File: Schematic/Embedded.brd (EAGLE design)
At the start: 98.7 x 81.3 mm, 19 parts, among them T1 2N3904, T2 2N3904, T3 2N3904, T4 2N3904

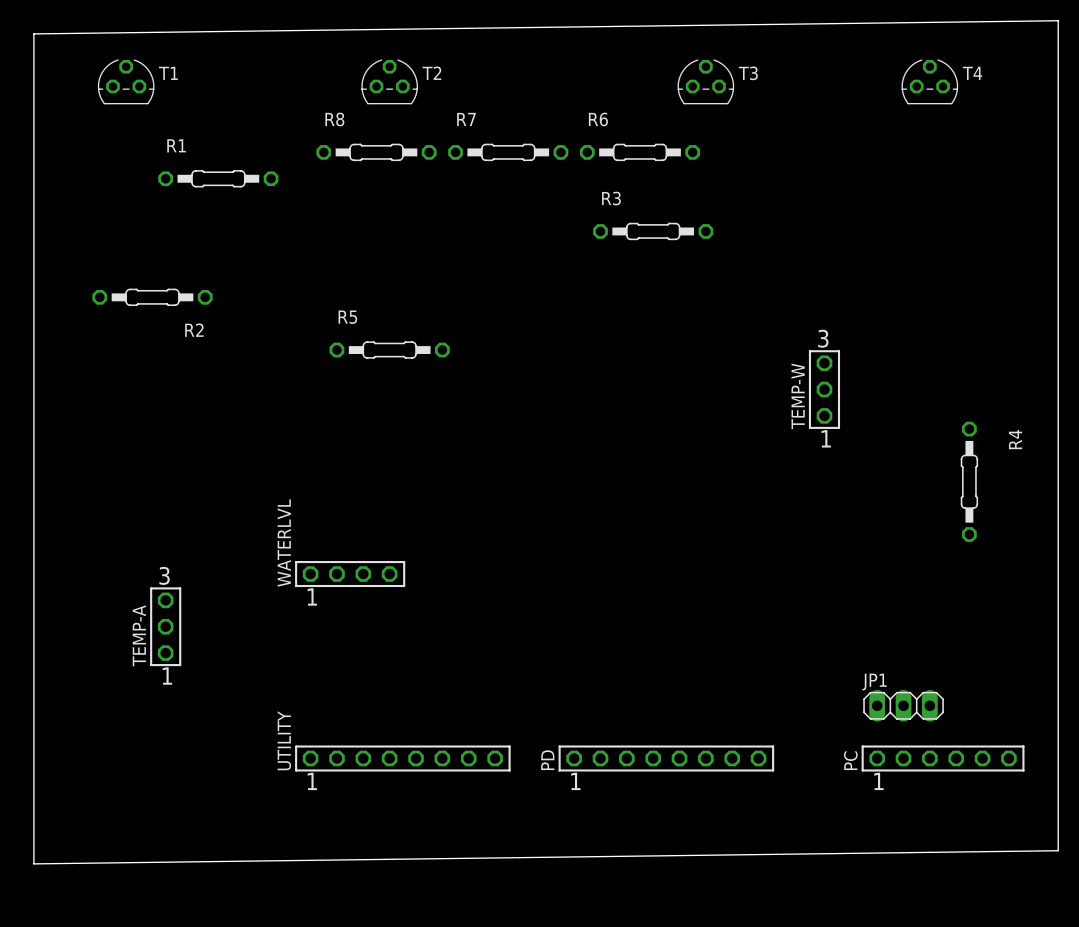
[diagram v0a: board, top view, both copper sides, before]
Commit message: Added Relay Definitions
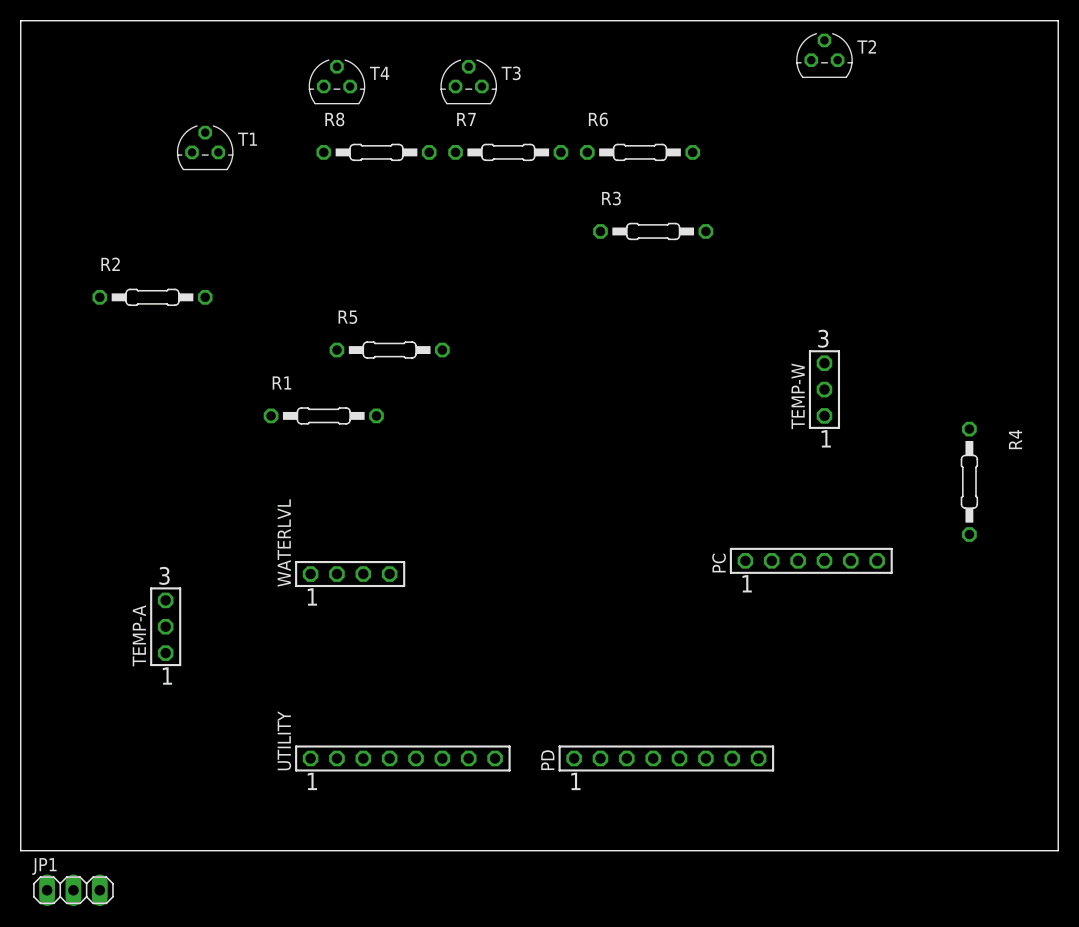
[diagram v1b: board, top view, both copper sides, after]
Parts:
- moved JP1 82.0 mm to (5.08, -3.81)
- moved T4 57.1 mm to (30.5, 73.7)
- moved T2 42.0 mm to (77.5, 76.2)
- moved R1 25.0 mm to (29.2, 41.9)
- moved PC 22.9 mm to (76.2, 27.9)
- moved T3 22.9 mm to (43.2, 73.7)
- moved T1 9.92 mm to (17.8, 67.3)
- turned R2 to 0 degrees
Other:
- board size 98.7 x 81.3 mm -> 100 x 80 mm

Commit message: I believe that I finally Finished.
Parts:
- R2: value 1k -> 10k
- R3: value 10k -> 1k
- moved JP1 89.6 mm to (90.2, 24.1)
- moved R4 66.3 mm to (29.2, 58.4)
- moved T4 52.1 mm to (82.5, 71.1)
- moved R8 46.6 mm to (80.0, 58.4), turned to 270 degrees
- moved TEMP-W 46.2 mm to (38.1, 20.3), turned to 270 degrees
- moved T2 46.0 mm to (31.8, 71.1)
- moved R7 39.1 mm to (85.1, 58.4), turned to 270 degrees
- moved R5 29.7 mm to (63.5, 58.4), turned to 270 degrees
- moved PD 28.1 mm to (53.3, 35.6)
- moved WATERLVL 26.2 mm to (57.1, 20.3), turned to 180 degrees
- moved R3 25.4 mm to (35.6, 58.4), turned to 90 degrees
- moved PC 24.4 mm to (87.6, 6.35)
- moved R1 21.6 mm to (15.2, 58.4), turned to 270 degrees
- moved UTILITY 20.5 mm to (57.1, 6.35)
- moved T3 16.7 mm to (59.7, 71.1)
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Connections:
- removed net N$14: R5.2
- removed net N$19: R7.2
- removed net N$9: R3.1
- new net 5V: R3.1, R5.2, R7.2
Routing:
- net GND: track 0.00 -> 209.7 mm
- net +5V: track 0.00 -> 130.5 mm
- net 5V: track 0.00 -> 53.4 mm
- net D4: track 0.00 -> 50.6 mm
- net D1: track 0.00 -> 37.6 mm
- net D5: track 0.00 -> 35.5 mm
- net D7: track 0.00 -> 25.1 mm
- net A0: track 0.00 -> 22.5 mm
- net D2: track 0.00 -> 21.0 mm
- net D6: track 0.00 -> 18.4 mm
- net D3: track 0.00 -> 15.8 mm
- net N$1: track 0.00 -> 10.8 mm
- net N$16: track 0.00 -> 10.6 mm
- net N$6: track 0.00 -> 10.6 mm
- net N$11: track 0.00 -> 10.1 mm
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
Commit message: Fixed Disconnected 5V
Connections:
- removed net 5V: R3.1, R5.2, R7.2
- net +5V: now also R3.1, R5.2, R7.2
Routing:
- net +5V: track 130.5 -> 208.1 mm
- net 5V: track 53.4 -> 0.00 mm
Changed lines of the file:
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@@
 <drawing>
 <settings>
-<setting alwaysvectorfont="yes"/>
+<setting alwaysvectorfont="no"/>
 <setting verticaltext="up"/>
 </settings>
@@
 <wire x1="38.1" y1="20.32" x2="38.1" y2="20.066" width="0.1524" layer="1"/>
 <wire x1="41.5036" y1="16.6624" x2="38.1" y2="20.066" width="0.1524" layer="1"/>
-<wire x1="59.8424" y1="16.6624" x2="41.5036" y2="16.6624" width="0.1524" layer="1"/>
-<wire x1="58.42" y1="20.32" x2="57.3024" y2="19.2024" width="0.1524" layer="1"/>
-<wire x1="60.96" y1="15.5448" x2="60.96" y2="6.35" width="0.1524" layer="1"/>
-<wire x1="57.3024" y1="19.2024" x2="59.8424" y2="16.6624" width="0.1524" layer="1"/>
-<wire x1="59.8424" y1="16.6624" x2="60.96" y2="15.5448" width="0.1524" layer="1"/>
+<wire x1="58.42" y1="16.6624" x2="41.5036" y2="16.6624" width="0.1524" layer="1"/>
+<wire x1="60.96" y1="14.2748" x2="60.96" y2="6.35" width="0.1524" layer="1"/>
+<wire x1="58.42" y1="20.32" x2="58.42" y2="16.6624" width="0.1524" layer="1"/>
+<wire x1="58.5724" y1="16.6624" x2="60.96" y2="14.2748" width="0.1524" layer="1"/>
 <wire x1="90.17" y1="24.13" x2="90.17" y2="21.9456" width="0.1524" layer="1"/>
-<wire x1="90.17" y1="21.9456" x2="83.7692" y2="15.5448" width="0.1524" layer="1"/>
-<wire x1="60.96" y1="15.5448" x2="83.7692" y2="15.5448" width="0.1524" layer="1"/>
+<wire x1="90.17" y1="21.9456" x2="82.4992" y2="14.2748" width="0.1524" layer="1"/>
+<wire x1="60.96" y1="14.2748" x2="82.4992" y2="14.2748" width="0.1524" layer="1"/>
 <wire x1="17.78" y1="21.59" x2="17.78" y2="21.336" width="0.1524" layer="16"/>
 <wire x1="21.082" y1="18.034" x2="17.78" y2="21.336" width="0.1524" layer="16"/>
 <wire x1="38.1" y1="20.32" x2="38.1" y2="18.034" width="0.1524" layer="16"/>
 <wire x1="38.1" y1="18.034" x2="21.082" y2="18.034" width="0.1524" layer="16"/>
+<contactref element="R3" pad="1"/>
+<contactref element="R5" pad="2"/>
+<wire x1="56.7944" y1="55.6768" x2="54.4576" y2="53.34" width="0.1524" layer="1"/>
+<wire x1="61.0616" y1="55.6768" x2="56.7944" y2="55.6768" width="0.1524" layer="1"/>
+<wire x1="63.3984" y1="53.34" x2="61.0616" y2="55.6768" width="0.1524" layer="1"/>
+<wire x1="63.3984" y1="53.34" x2="63.5" y2="53.34" width="0.1524" layer="1"/>
+<wire x1="15.24" y1="53.34" x2="24.13" y2="53.34" width="0.1524" layer="1"/>
+<wire x1="24.13" y1="53.34" x2="26.67" y2="55.88" width="0.1524" layer="1"/>
+<wire x1="33.02" y1="55.88" x2="35.56" y2="53.34" width="0.1524" layer="1"/>
+<wire x1="26.67" y1="55.88" x2="33.02" y2="55.88" width="0.1524" layer="1"/>
+<wire x1="35.56" y1="53.34" x2="54.4576" y2="53.34" width="0.1524" layer="1"/>
+<wire x1="58.42" y1="20.32" x2="58.5724" y2="20.1676" width="0.1524" layer="1"/>
+<wire x1="58.5724" y1="20.1676" x2="58.5724" y2="16.6624" width="0.1524" layer="1"/>
+<contactref element="R7" pad="2"/>
+<wire x1="83.9216" y1="53.34" x2="85.09" y2="53.34" width="0.1524" layer="1"/>
+<wire x1="81.5848" y1="55.6768" x2="83.9216" y2="53.34" width="0.1524" layer="1"/>
+<wire x1="65.8876" y1="55.6768" x2="81.5848" y2="55.6768" width="0.1524" layer="1"/>
+<wire x1="63.5508" y1="53.34" x2="65.8876" y2="55.6768" width="0.1524" layer="1"/>
+<wire x1="63.5" y1="53.34" x2="63.5508" y2="53.34" width="0" layer="19" extent="1-1"/>
 </signal>
 <signal name="GND">
@@
 <wire x1="81.3816" y1="8.9916" x2="81.3816" y2="6.4008" width="0.1524" layer="1"/>
 <wire x1="92.71" y1="24.13" x2="92.71" y2="20.32" width="0.1524" layer="1"/>
-<wire x1="92.71" y1="20.32" x2="81.3816" y2="8.9916" width="0.1524" layer="1"/>
+<wire x1="92.71" y1="20.32" x2="88.265" y2="15.875" width="0.1524" layer="1"/>
+<wire x1="88.265" y1="15.875" x2="81.3816" y2="8.9916" width="0.1524" layer="1"/>
 <wire x1="81.3816" y1="6.4008" x2="81.28" y2="6.35" width="0.1524" layer="1"/>
-</signal>
-<signal name="5V">
-<contactref element="R3" pad="1"/>
-<contactref element="R5" pad="2"/>
-<contactref element="R7" pad="2"/>
-<wire x1="54.4576" y1="53.34" x2="35.56" y2="53.34" width="0.1524" layer="1"/>
-<wire x1="56.7944" y1="55.6768" x2="54.4576" y2="53.34" width="0.1524" layer="1"/>
-<wire x1="61.0616" y1="55.6768" x2="56.7944" y2="55.6768" width="0.1524" layer="1"/>
-<wire x1="63.3984" y1="53.34" x2="61.0616" y2="55.6768" width="0.1524" layer="1"/>
-<wire x1="63.3984" y1="53.34" x2="63.5" y2="53.34" width="0.1524" layer="1"/>
-<wire x1="83.9216" y1="53.34" x2="85.09" y2="53.34" width="0.1524" layer="1"/>
-<wire x1="81.5848" y1="55.6768" x2="83.9216" y2="53.34" width="0.1524" layer="1"/>
-<wire x1="65.8876" y1="55.6768" x2="81.5848" y2="55.6768" width="0.1524" layer="1"/>
-<wire x1="63.5508" y1="53.34" x2="65.8876" y2="55.6768" width="0.1524" layer="1"/>
-<wire x1="63.5508" y1="53.34" x2="63.5" y2="53.34" width="0.1524" layer="1"/>
 </signal>
 </signals>
@@
 <mfgpreviewcolor name="substratecolor" color="0xFF786E46"/>
 </mfgpreviewcolors>
+<errors>
+</errors>
 </board>
 </drawing>

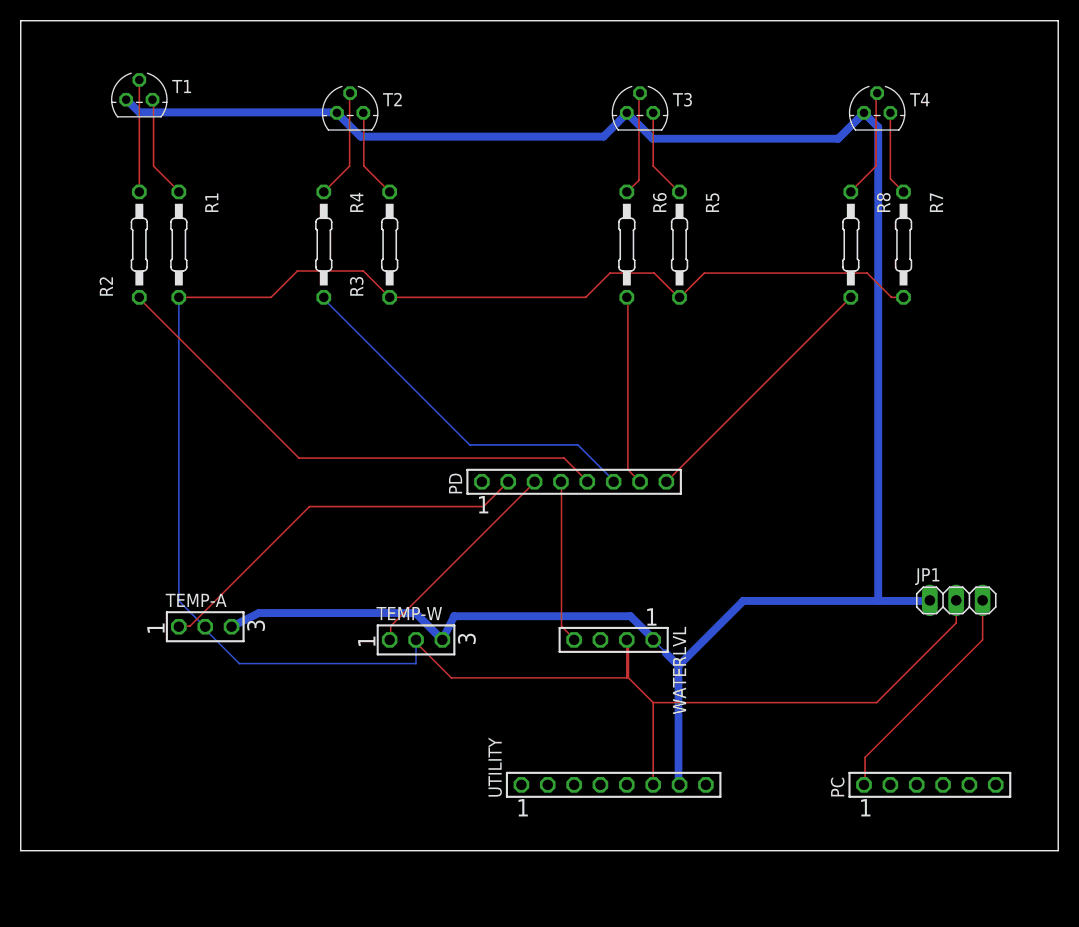
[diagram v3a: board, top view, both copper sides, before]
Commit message: Checked Wires
Found a GND wire that is thin to a point. Unfortunately, the PCB is already  printed.
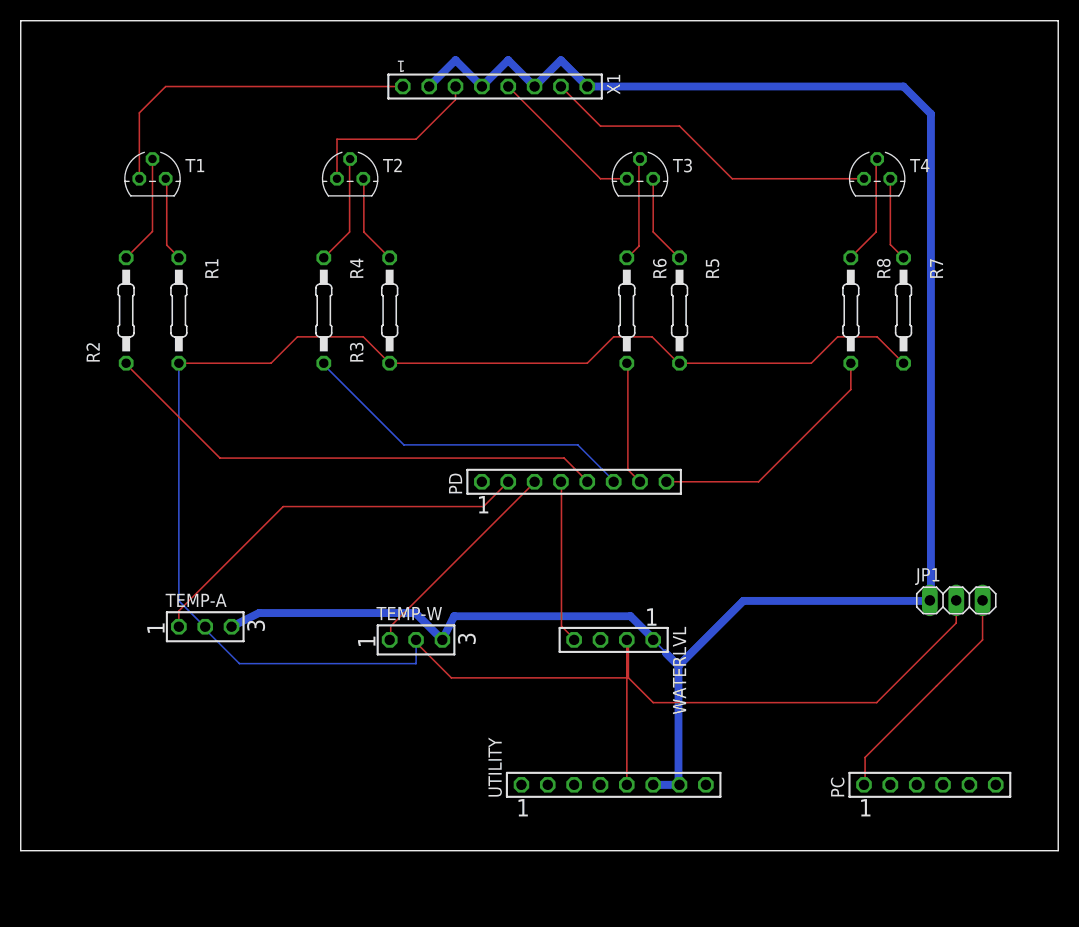
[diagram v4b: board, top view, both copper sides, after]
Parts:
- added X1: TSW-108-07-G-S, con-samtec:TSW-108-XX-G-S
- moved T1 7.73 mm to (12.7, 64.8)
- moved R2 6.48 mm to (10.2, 52.1)
- moved T2 6.35 mm to (31.8, 64.8)
- moved T3 6.35 mm to (59.7, 64.8)
- moved T4 6.35 mm to (82.5, 64.8)
- moved R1 6.35 mm to (15.2, 52.1)
- moved R3 6.35 mm to (35.6, 52.1)
- moved R4 6.35 mm to (29.2, 52.1)
- moved R5 6.35 mm to (63.5, 52.1)
- moved R6 6.35 mm to (58.4, 52.1)
- moved R7 6.35 mm to (85.1, 52.1)
- moved R8 6.35 mm to (80.0, 52.1)
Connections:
- new net P1: T1.3, X1.1
- new net P2: T2.3, X1.3
- new net P3: T3.3, X1.5
- new net P4: T4.3, X1.7
- net +5V: now also UTILITY.5; no longer UTILITY.6
- net GND: now also UTILITY.6, X1.2, X1.4, X1.6, X1.8; no longer T1.3, T2.3, T3.3, T4.3
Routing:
- net P4: track 0.00 -> 32.9 mm
- net P1: track 0.00 -> 32.8 mm
- net P2: track 0.00 -> 18.1 mm
- net GND: track 209.7 -> 191.7 mm
- net P3: track 0.00 -> 15.1 mm
- net D6: track 18.4 -> 12.0 mm
- net D5: track 35.5 -> 32.8 mm
- net N$2: track 10.0 -> 8.21 mm
- net D4: track 50.6 -> 49.3 mm
- net D7: track 25.1 -> 24.0 mm
- net D1: track 37.6 -> 38.4 mm
